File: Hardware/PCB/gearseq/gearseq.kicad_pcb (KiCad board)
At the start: 2 copper layers, 209.5 x 165 mm, 77 parts, among them J1 AudioJack2_SwitchT, J10 Conn_01x11, J11 Conn_01x04, J12 AudioJack2, J13 AudioJack2, J14 Conn_01x11, J15 2_pin_Molex_connector, J16 2_pin_Molex_connector, J2 AudioJack2_SwitchT, J3 AudioJack2, J4 AudioJack2, J5 Synth_power_2x5, J6 2_pin_Molex_header, J7 2_pin_Molex_header, J8 AudioJack2_SwitchT, J9 AudioJack2_SwitchT, SW1 SW_Push_black, SW2 SW_Push_red, U1 MCP6002-xP, U2 L78L05_TO92

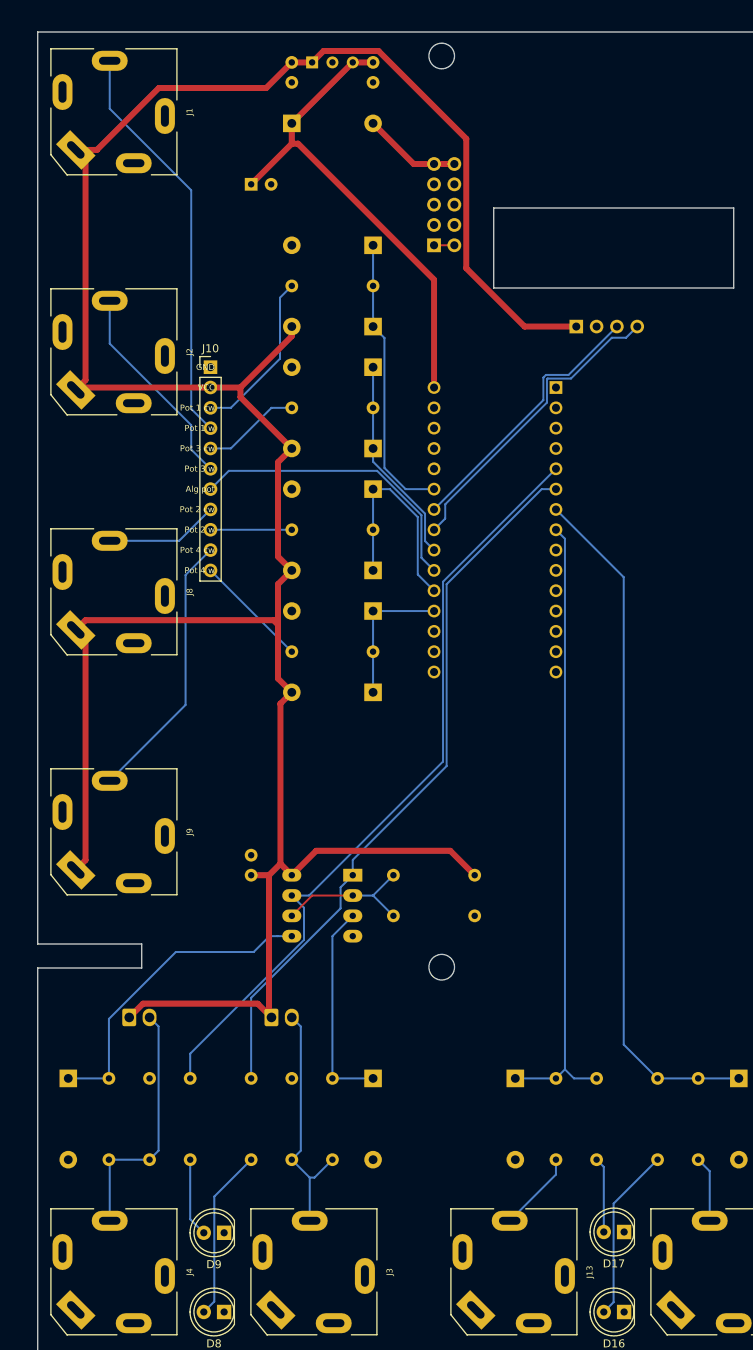
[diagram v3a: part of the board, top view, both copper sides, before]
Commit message: Revise clock and reset inputs, shift board positions
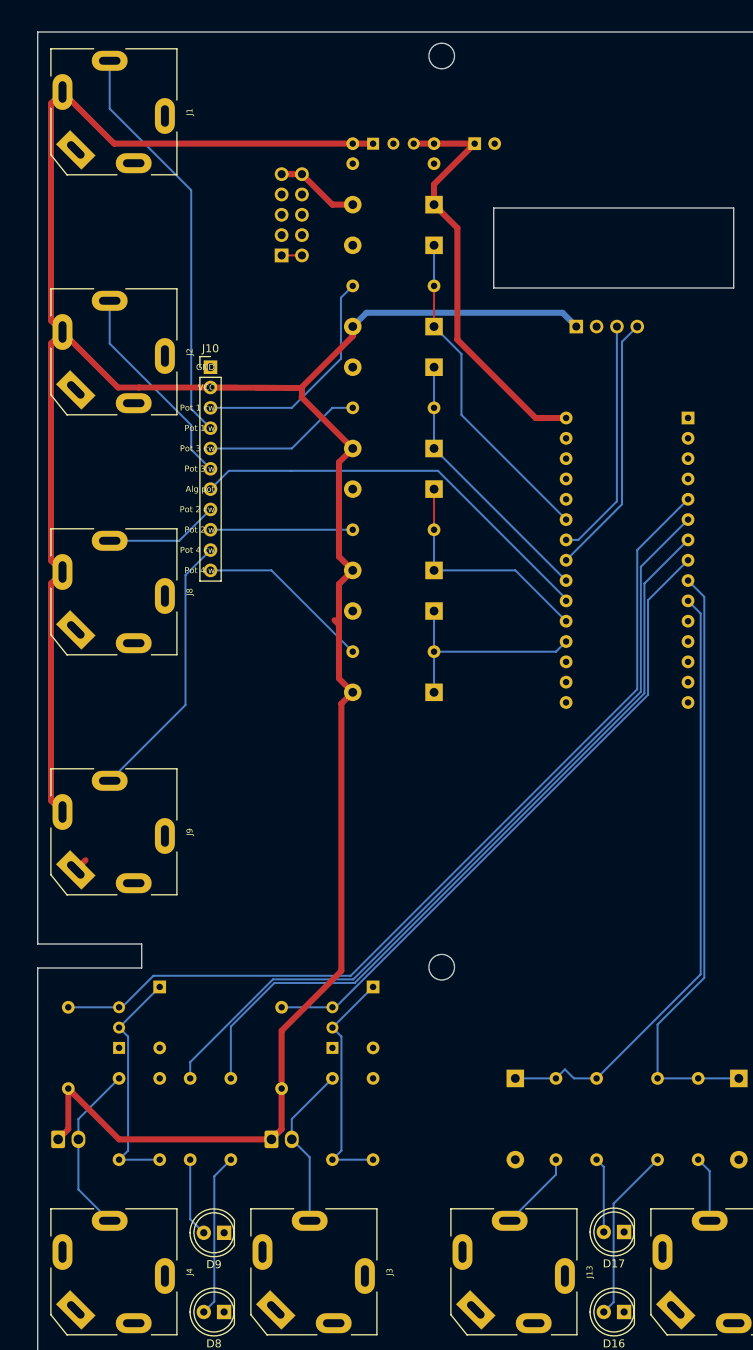
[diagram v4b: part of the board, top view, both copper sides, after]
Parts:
- removed C4: 100nF, ao_tht:C_Disc_D3.0mm_W1.6mm_P2.50mm
- removed U1: MCP6002-xP, ao_tht:DIP-8_W7.62mm_Socket_LongPads
- added Q1: 2N3904, ao_tht:TO-92_Inline_Wide, B.Cu at (62.8, 149.0)
- added Q2: 2N3904, ao_tht:TO-92_Inline_Wide, B.Cu at (36.2, 149.0)
- A1: footprint Module:Arduino_Nano -> ao_tht:Arduino_Nano
- C3: value 100nF -> 10nF
- D1, D2: value 1N4733A -> 1N4148; footprint ao_tht:D_DO-41_SOD81_P10.16mm_Horizontal -> ao_tht:D_DO-35_SOD27_P7.62mm_Horizontal
- R3, R4: value 1k -> 1M
- R9: value 100k -> 10k
- moved GRAF4 90.9 mm to (92.7, 126.0)
- moved R10 46.0 mm to (29.8, 154.1), turned to 90 degrees
- moved GRAF3 41.4 mm to (62.7, 121.0)
- moved R9 36.0 mm to (56.5, 154.1), turned to 90 degrees
- moved C1 28.4 mm to (80.6, 36.0)
- moved D3 20.5 mm to (75.5, 43.6), turned to 180 degrees
- moved J5 19.1 mm to (56.5, 49.9)
- moved J7 17.6 mm to (28.6, 160.4)
- moved A1 16.9 mm to (107.3, 70.2)
- moved D2 16.2 mm to (41.2, 141.4)
- moved J6 15.2 mm to (55.2, 160.4)
- moved C2 12.7 mm to (75.5, 36.0)
- moved U2 12.7 mm to (67.9, 36.0)
- moved C3 12.7 mm to (65.4, 36.0)
- moved R4 12.0 mm to (41.2, 163.0), turned to 90 degrees
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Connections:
- net /CLOCK_LED renamed Net-(D9-Pad2)
- net /RESET1_LED renamed Net-(D8-Pad2)
- A1 pad 10: Net-(A1-Pad10) -> PER_OUT
- A1 pad 6: RESET -> CLOCK_LED
- A1 pad 7: SEQ_OUT -> RES_LED
- A1 pad 8: PER_OUT -> RESET
- A1 pad 9: Net-(A1-Pad9) -> SEQ_OUT
- J1 pad S: +5V -> GND
- J1 pad TN: GND -> +5V
- J2 pad S: +5V -> GND
- J2 pad TN: GND -> +5V
- J8 pad S: +5V -> GND
- J8 pad TN: GND -> +5V
- J9 pad S: +5V -> GND
- J9 pad TN: GND -> +5V
- R1 pad 1: /RESET_J -> Net-(D1-Pad1)
- R1 pad 2: GND -> /RESET_J
- R10 pad 1: /VREF -> +5V
- R10 pad 2: GND -> CLOCK_IN
- R2 pad 1: /CLK_IN_J -> Net-(D2-Pad1)
- R2 pad 2: GND -> /CLK_IN_J
- R3 pad 2: /RESET_J -> GND
- R4 pad 2: /CLK_IN_J -> GND
- R7 pad 2: RESET -> RES_LED
- R8 pad 2: CLOCK_IN -> CLOCK_LED
- R9 pad 2: /VREF -> RESET
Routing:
- net CLOCK_LED: track 0.00 -> 101.5 mm
- net RES_LED: track 0.00 -> 96.9 mm
- net /VREF: track 18.4 -> 0.00 mm
- net CLOCK_IN: track 97.7 -> 114.0 mm
- net POT_ALG: track 37.2 -> 52.5 mm
- net SEQ_OUT: track 86.5 -> 75.7 mm
- net /RESET_J: track 31.0 -> 20.8 mm
- net Net-(D2-Pad1): track 39.7 -> 29.7 mm
- net /CLK_IN_J: track 31.5 -> 21.5 mm
- net RESET: track 90.5 -> 80.9 mm
- net CV_4: track 17.8 -> 27.2 mm
- net +12V: track 61.3 -> 53.1 mm
- net POT_3_W: track 10.2 -> 17.8 mm
- net POT_2_W: track 12.3 -> 19.9 mm
- net POT_1_W: track 20.9 -> 28.6 mm
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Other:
- board text added: "Rich Holmes CC0 1.0 / Nov 2021 https://github.com/holmesrichards/gearseq"
- board text removed: "CC0"
- board text removed: "Rich Holmes 9/2021"
- board text removed: "https://github.com/holmesrichards/gearseq"

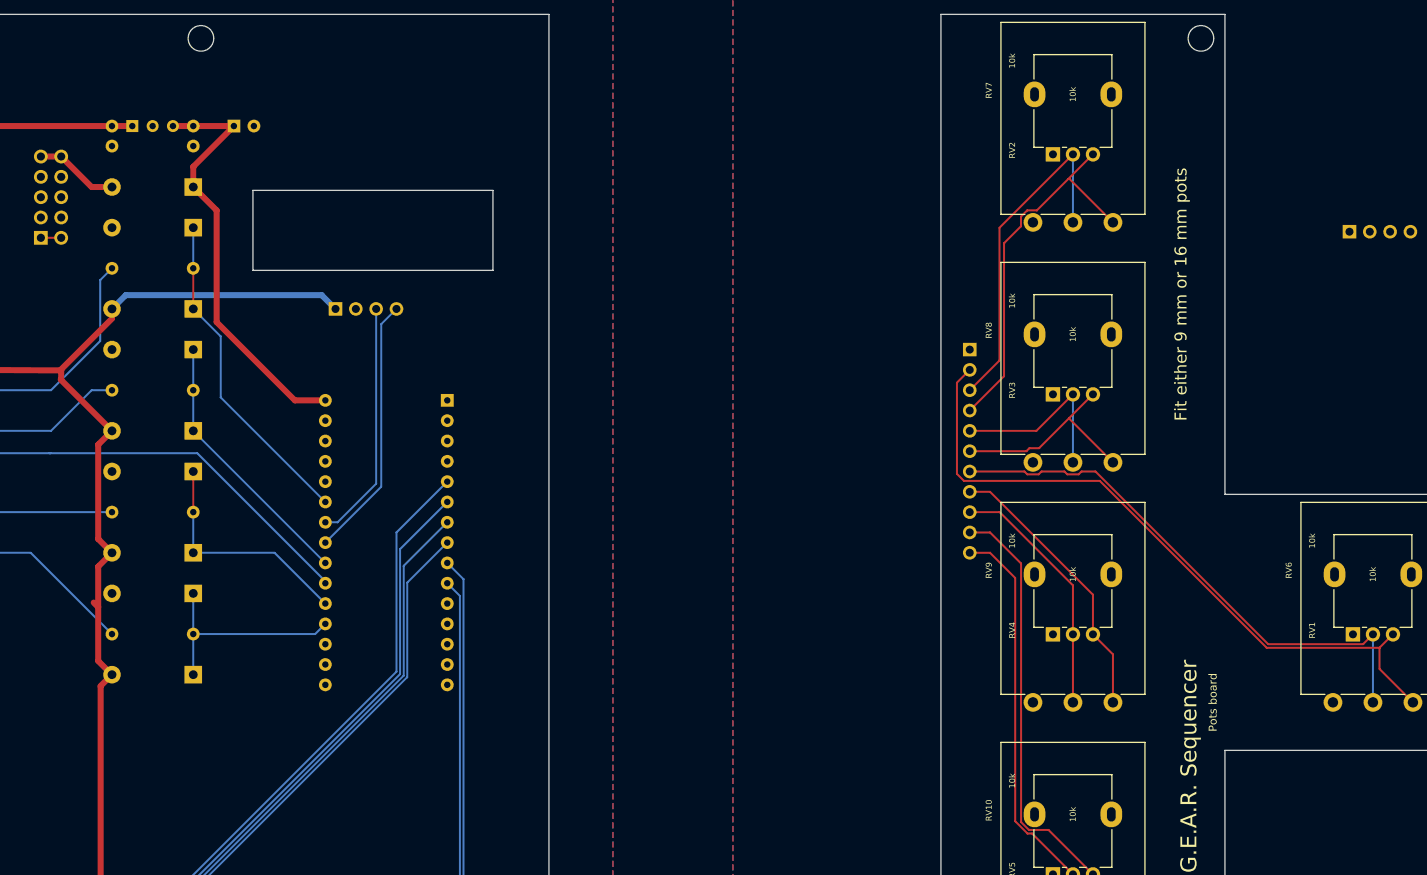
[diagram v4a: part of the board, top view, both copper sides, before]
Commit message: Add capacitors
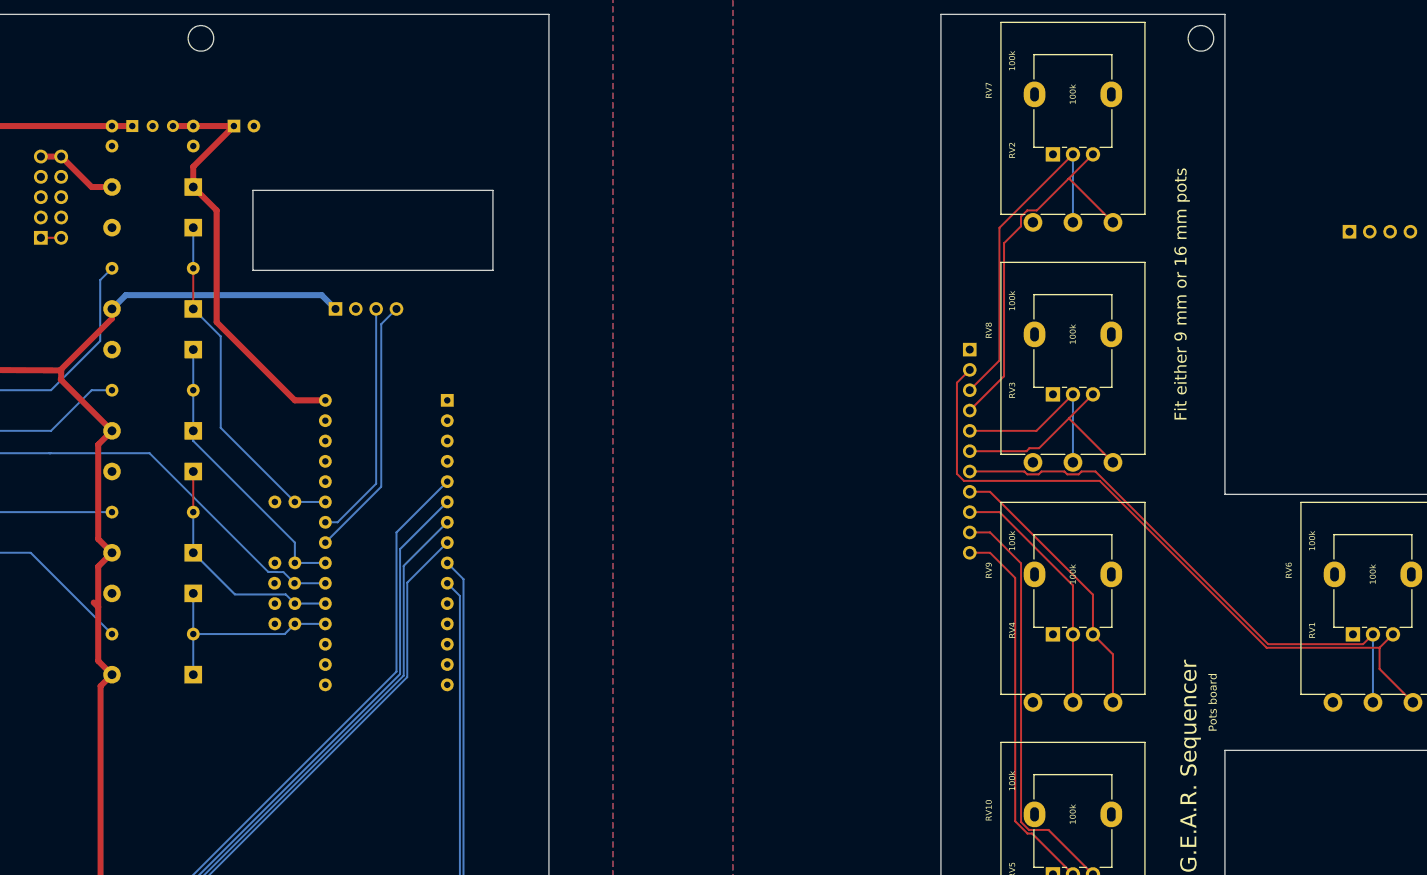
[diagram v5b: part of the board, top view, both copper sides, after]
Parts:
- added C4: 100nF, ao_tht:C_Disc_D3.0mm_W1.6mm_P2.50mm, B.Cu at (88.2, 83.0)
- added C5: 100nF, ao_tht:C_Disc_D3.0mm_W1.6mm_P2.50mm, B.Cu at (88.2, 90.6)
- added C6: 100nF, ao_tht:C_Disc_D3.0mm_W1.6mm_P2.50mm, B.Cu at (88.2, 95.7)
- added C7: 100nF, ao_tht:C_Disc_D3.0mm_W1.6mm_P2.50mm, B.Cu at (88.2, 98.2)
- added C8: 100nF, ao_tht:C_Disc_D3.0mm_W1.6mm_P2.50mm, B.Cu at (85.7, 93.1)
- RV1, RV10, RV2, RV3, RV4, RV5, RV6, RV7, RV8, RV9: value 10k -> 100k
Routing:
- net CV_2: track 33.5 -> 35.7 mm
- net CV_1: track 41.1 -> 43.4 mm

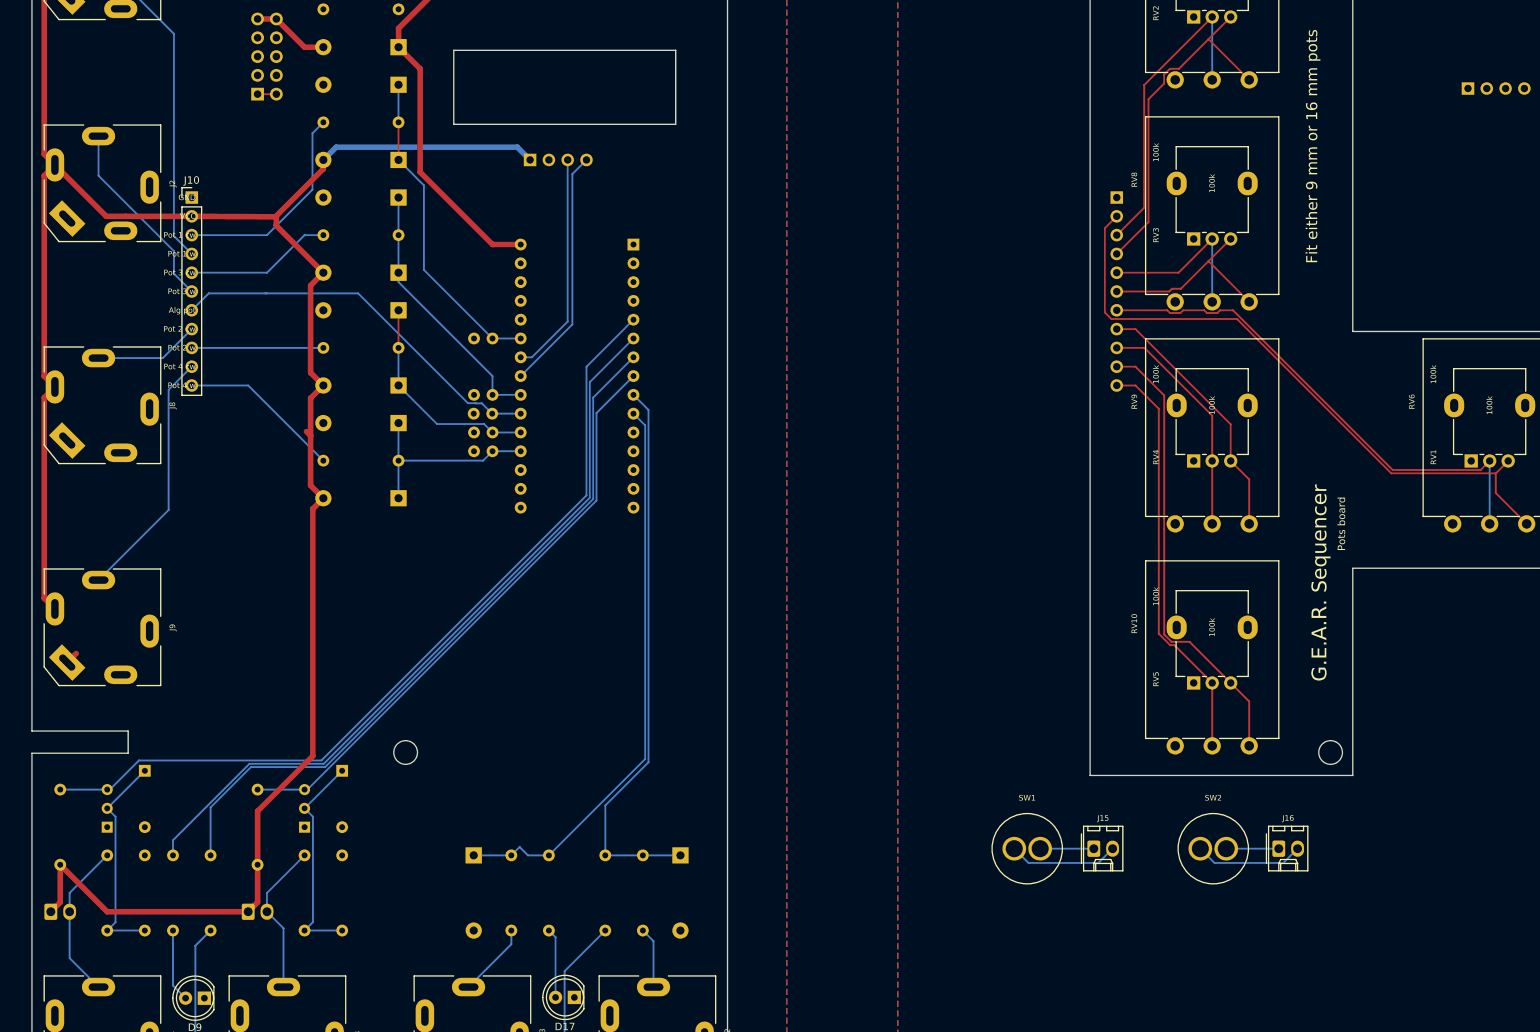
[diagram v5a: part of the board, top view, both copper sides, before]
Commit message: Add display blanking switch, stop Period output when None algo, flip OLED
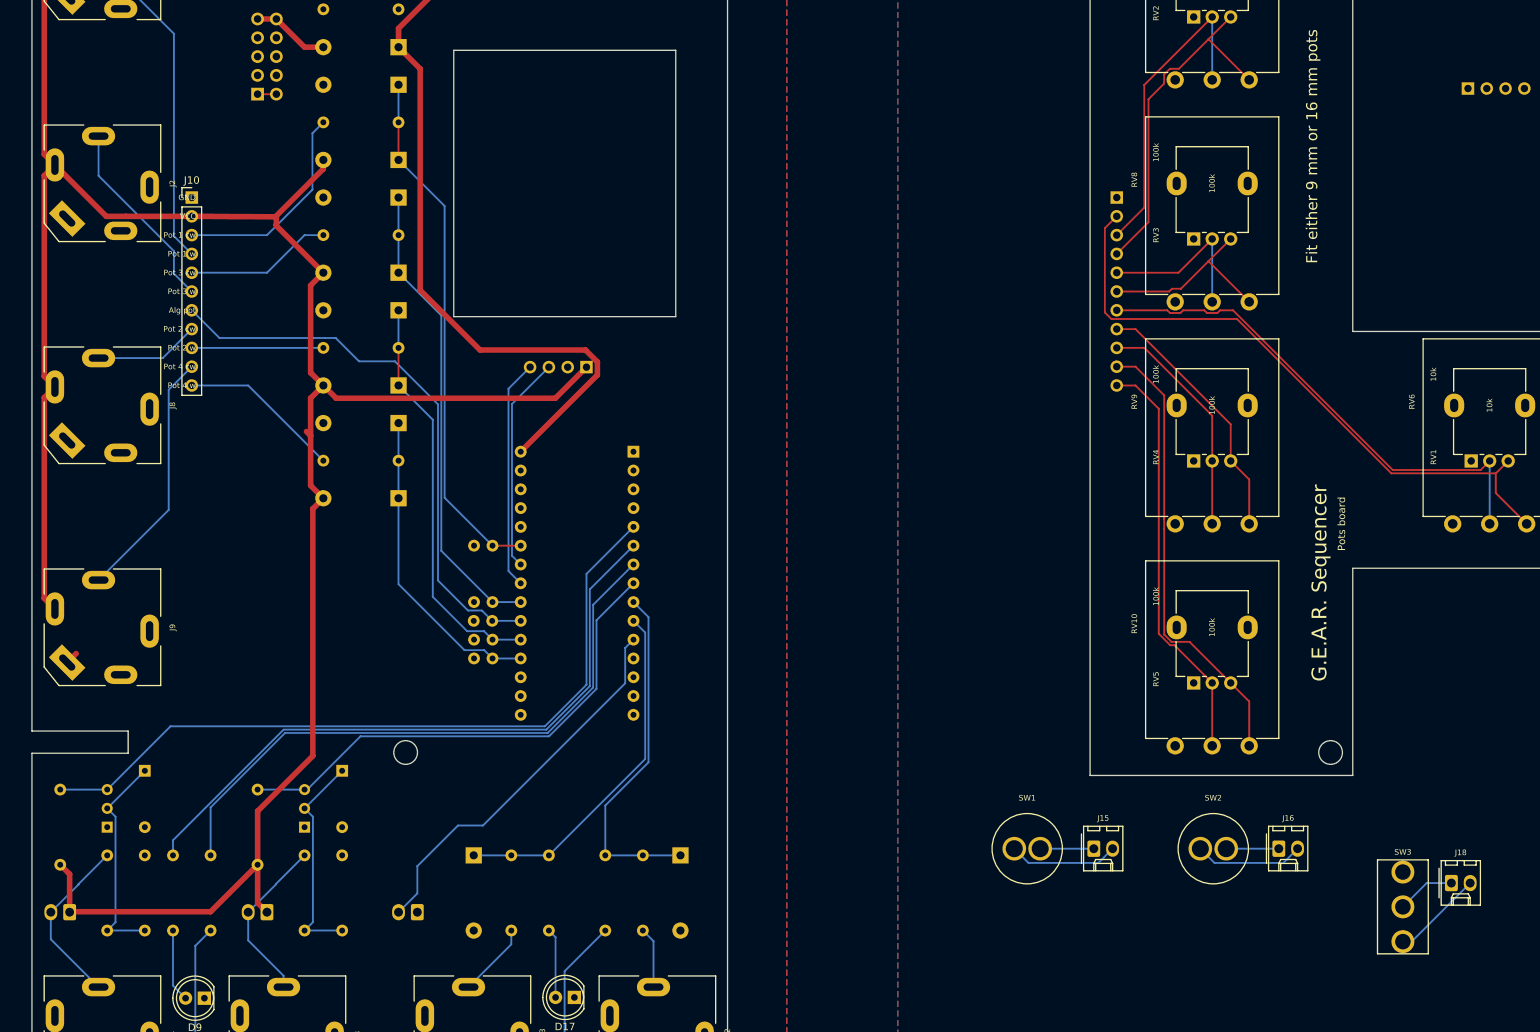
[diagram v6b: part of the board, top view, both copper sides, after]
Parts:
- added J17: 2_pin_Molex_header, ao_tht:Molex_KK-254_AE-6410-02A_1x02_P2.54mm_Vertical, B.Cu at (78.1, 160.5)
- added J18: 2_pin_Molex_connector, ao_tht:Molex_KK-254_AE-6410-02A_1x02_P2.54mm_Vertical, F.Cu at (217.8, 156.5)
- added SW3: SW_SPST, ao_tht:SPDT-toggle-switch-1M-series, F.Cu at (211.3, 159.8)
- RV1, RV6: value 100k -> 10k
- moved J11 29.0 mm to (100.9, 86.8), turned to 90 degrees
- moved GRAF4 28.7 mm to (64.0, 127.2)
- moved A1 28.0 mm to (107.3, 98.2)
- moved C4 28.0 mm to (88.2, 111.0)
- moved C5 28.0 mm to (88.2, 118.6)
- moved C6 28.0 mm to (88.2, 123.7)
- moved C7 28.0 mm to (88.2, 126.2)
- moved C8 28.0 mm to (85.7, 121.1)
- moved GRAF3 20.8 mm to (54.1, 102.0)
- moved J6 2.54 mm to (57.8, 160.5), turned to 180 degrees
- moved J7 2.54 mm to (31.1, 160.5), turned to 180 degrees
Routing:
- net Net-(A1-Pad11): track 0.00 -> 52.0 mm
- net +12V: track 53.1 -> 95.8 mm
- net PER_OUT: track 76.8 -> 47.9 mm
- net CV_2: track 35.7 -> 63.7 mm
- net SEQ_OUT: track 75.7 -> 47.7 mm
- net CV_1: track 43.4 -> 71.4 mm
- net CV_3: track 29.3 -> 54.9 mm
- net POT_ALG: track 52.4 -> 75.8 mm
- net CV_4: track 27.2 -> 42.4 mm
- net RES_LED: track 96.9 -> 83.8 mm
- net CLOCK_LED: track 101.5 -> 88.4 mm
- net CLOCK_IN: track 114.0 -> 101.0 mm
- net RESET: track 80.9 -> 68.2 mm
- net Net-(J18-Pad2): track 0.00 -> 12.4 mm
- net +5V: track 347.6 -> 356.4 mm
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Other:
- outline, holes or cut-outs redrawn
